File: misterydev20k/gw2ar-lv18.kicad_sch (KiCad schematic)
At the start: 55 parts, among them J3 JTAG, U10 TLV62569DBV, U11 TLV62569DBV, U5 GW2AR-LV18-QN88, U6 W25Q128JVS, U8 ME6211C33M5, U9 ME6211C33M5, Y2 27MHz

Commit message: Some dev board progress
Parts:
- removed JP4: VCCO_5, Jumper:SolderJumper-2_P1.3mm_Bridged_RoundedPad1.0x1.5mm, symbol Jumper:SolderJumper_2_Bridged
- removed JP5: VCC33, Jumper:SolderJumper-2_P1.3mm_Bridged_RoundedPad1.0x1.5mm, symbol Jumper:SolderJumper_2_Bridged
- removed JP6: +1V0, Jumper:SolderJumper-2_P1.3mm_Bridged_RoundedPad1.0x1.5mm, symbol Jumper:SolderJumper_2_Bridged
- JP3: value VCCO_4 -> ~{CFG}
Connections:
- net +1V0: now also FB2.2
- net VCC33: now also FB1.2
- net VCCO_4: now also C34.2, U8.5 (V_{OUT}); no longer JP3.2 (B)
- net VCCO_5: now also C36.2, U9.5 (V_{OUT})
- net at R40.2, U5.9 (IOR31B/~{RECONFIG}): now also JP3.2 (B)
- new net ~{CFG}: JP3.1 (A)
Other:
- note removed: "JP5, JP6 etc are used to isolate the FPGA during initial bringup."
- moved on the sheet: J3, R18

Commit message: More updates in dev20k
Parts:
- removed C37: 100nF, Capacitor_SMD:C_0402_1005Metric, symbol Device:C_Small
- removed C38: 10uF, Capacitor_SMD:C_0402_1005Metric, symbol Device:C_Small
- removed FB1: MPZ1608S101, Inductor_SMD:L_0603_1608Metric, symbol Device:FerriteBead
- removed L1: 2.2uH, Inductor_SMD:L_0805_2012Metric, symbol Device:L
- removed R36: 68k, Resistor_SMD:R_0402_1005Metric, symbol Device:R_Small
- removed R37: 15k, Resistor_SMD:R_0402_1005Metric, symbol Device:R_Small
- removed U10: TLV62569DBV, Package_TO_SOT_SMD:SOT-23-5, symbol Regulator_Switching:TLV62569DBV
- added C4, C46, C47, C48, C49, C50: 100nF, Capacitor_SMD:C_0402_1005Metric, symbol Device:C_Small
- added R26, R52: 22, Resistor_SMD:R_0402_1005Metric, symbol Device:R_Small
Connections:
- net GND: now also C4.1, C46.1, C47.1, C48.1, C49.1, C50.1
- net SD_CLK: now also R26.2, R52.2; no longer JP13.1 (A), JP13.2 (B)
- net VCC33: no longer C15.1, C27.1, R29.2, R31.2, R32.2, U5.12 (VCCX/VCC0_2/6/7), U5.3 (VCCX/VCC0_2/6/7), U5.58 (VCC0_3), U5.64 (VCCX/VCC0_2/6/7), U5.67 (VCC0_1), U5.78 (VCC0_0), U6.8 (VCC), Y2.1 (~{ST}), Y2.4 (Vcc)
- new net: JP13.1 (A), R26.1
- new net +3.3V: C15.1, C27.1, C4.2, C46.2, C47.2, C48.2, C49.2, C50.2, R29.2, R31.2, R32.2, U5.12 (VCCX/VCC0_2/6/7), U5.3 (VCCX/VCC0_2/6/7), U5.58 (VCC0_3), U5.64 (VCCX/VCC0_2/6/7), U5.67 (VCC0_1), U5.78 (VCC0_0), U6.8 (VCC), Y2.1 (~{ST}), Y2.4 (Vcc)
- new net Interfaces/SD_CLK: JP13.2 (B), R52.1
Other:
- note removed: "https://github.com/TomSimkin/UART_Verilog/blob/main/Tang_Nano_20K_3921_Schematics.pdf"
- moved on the sheet: C39, C40, FB2, L2, R38, R39, U11

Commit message: Update missing files
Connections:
- net SD_CLK: no longer R26.2
- new net SD_CLK_PI: R26.2
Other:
- sheet Interfaces ports: added ~{SD_DET}; removed none
- moved on the sheet: JP11, JP12, JP13, JP14, R26, R52

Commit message: Another board update
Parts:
- removed C40: 10uF, Capacitor_SMD:C_0402_1005Metric, symbol Device:C_Small
- removed FB2: MPZ1608S101, Inductor_SMD:L_0603_1608Metric, symbol Device:FerriteBead
- removed L2: 2.2uH, Inductor_SMD:L_0805_2012Metric, symbol Device:L
- removed U11: TLV62569DBV, Package_TO_SOT_SMD:SOT-23-5, symbol Regulator_Switching:TLV62569DBV
- removed U8, U9: ME6211C33M5, Package_TO_SOT_SMD:SOT-23-5, symbol Regulator_Linear:ME6211C33M5
- added C37: 22pF, Capacitor_SMD:C_0402_1005Metric, symbol Device:C_Small
- added C38: 22uF, Capacitor_SMD:C_0603_1608Metric, symbol Device:C_Small
- added L1: 3.3uH, Inductor_SMD:L_Sunlord_MWSA0402S, symbol Device:L
- added R37: 47k, Resistor_SMD:R_0402_1005Metric, symbol Device:R_Small
- added R56: 18k 1%, Resistor_SMD:R_0402_1005Metric, symbol Device:R_Small
- added U8: SY8113BADC, Package_TO_SOT_SMD:TSOT-23-6, symbol Regulator_Switching:LM2842Y
- C33: value 100nF -> 10uF; footprint Capacitor_SMD:C_0402_1005Metric -> Capacitor_SMD:C_0603_1608Metric; LCSC C1525 -> C52923
- C34, C39: footprint Capacitor_SMD:C_0402_1005Metric -> Capacitor_SMD:C_0603_1608Metric
- R38: value 10k -> 30k; LCSC (none) -> C11702
- R39: value 15k -> 12k 1%
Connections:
- net +1V0: now also C39.1, R39.2, C37.2, C38.1, L1.2
- net +3.3V: now also C16.2, C17.2, U5.23 (VCC0_5), U5.44 (VCC0_4)
- net +5V: now also C33.1, C34.1, R37.2, U8.5 (VIN); no longer C33.2, C35.2, C39.2
- net GND: now also C33.2, C34.2, C39.2, R38.1, C38.2, R56.1, U8.2 (GND); no longer C33.1, C34.1, C36.1, C39.1, R39.2
- net at R38.2: now also C35.2, R37.1, U8.4 (EN); no longer R39.1
- removed net VCCO_4: C17.2, C34.2, U5.44 (VCC0_4)
- removed net VCCO_5: C16.2, C36.2, U5.23 (VCC0_5)
- new net: C37.1, R39.1, R56.2, U8.3 (FB)
- new net: C36.1, U8.1 (BOOST)
- new net: C36.2, L1.1, U8.6 (SW)
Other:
- note added: "Vout = 0.6 * (1+R1/R2)"
- note removed: "or MT3520B"
- moved on the sheet: C4, C46, C47, C48, C49, C50

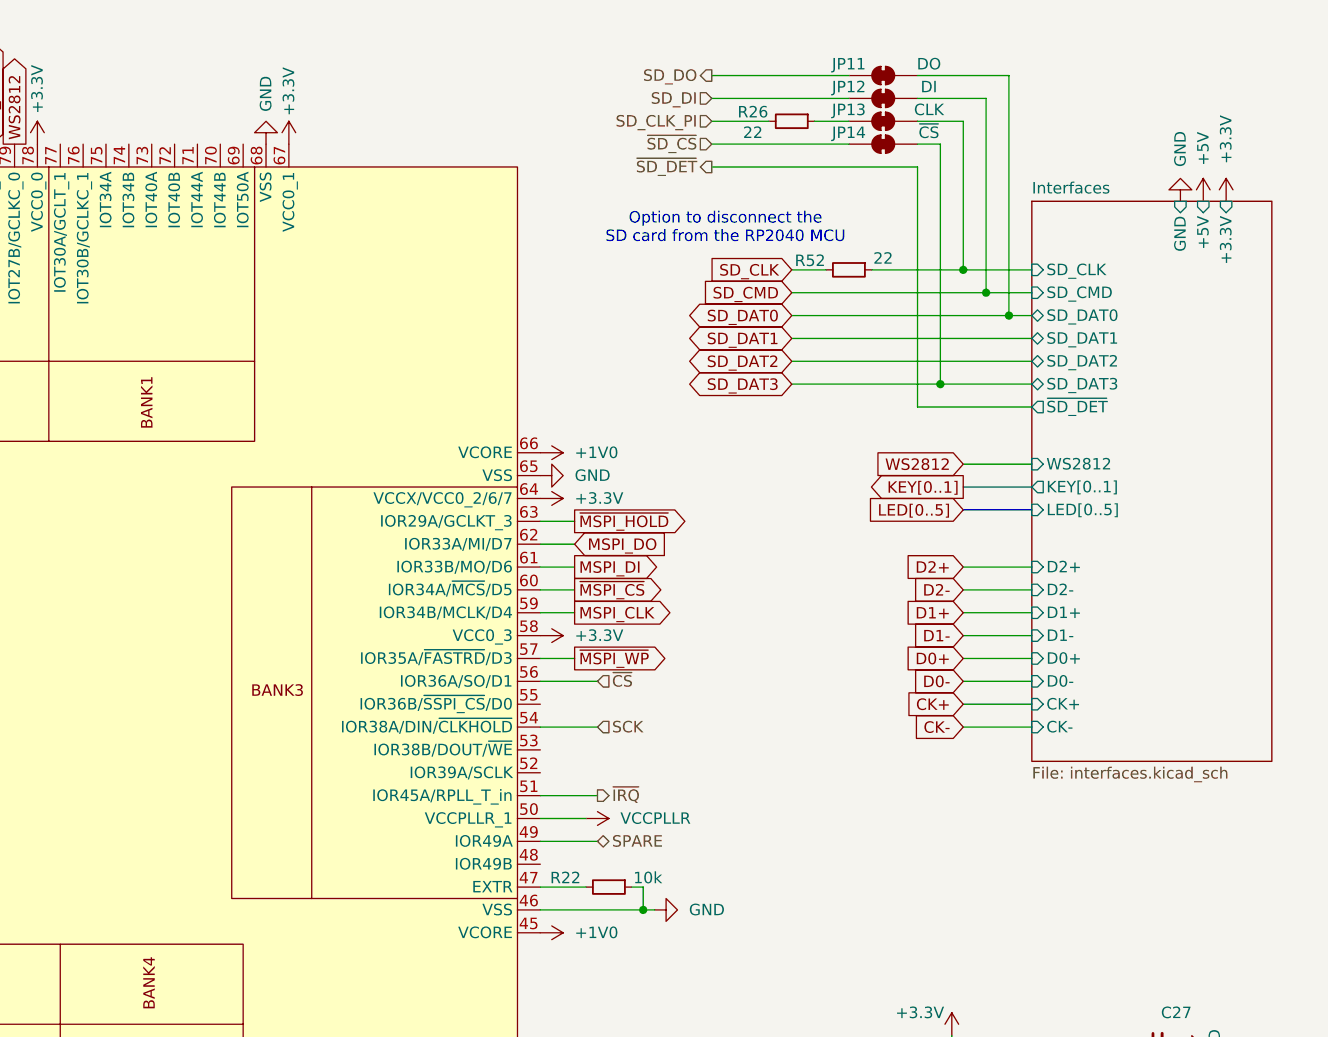
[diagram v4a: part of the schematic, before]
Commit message: Add grove connector for MIDI/UART
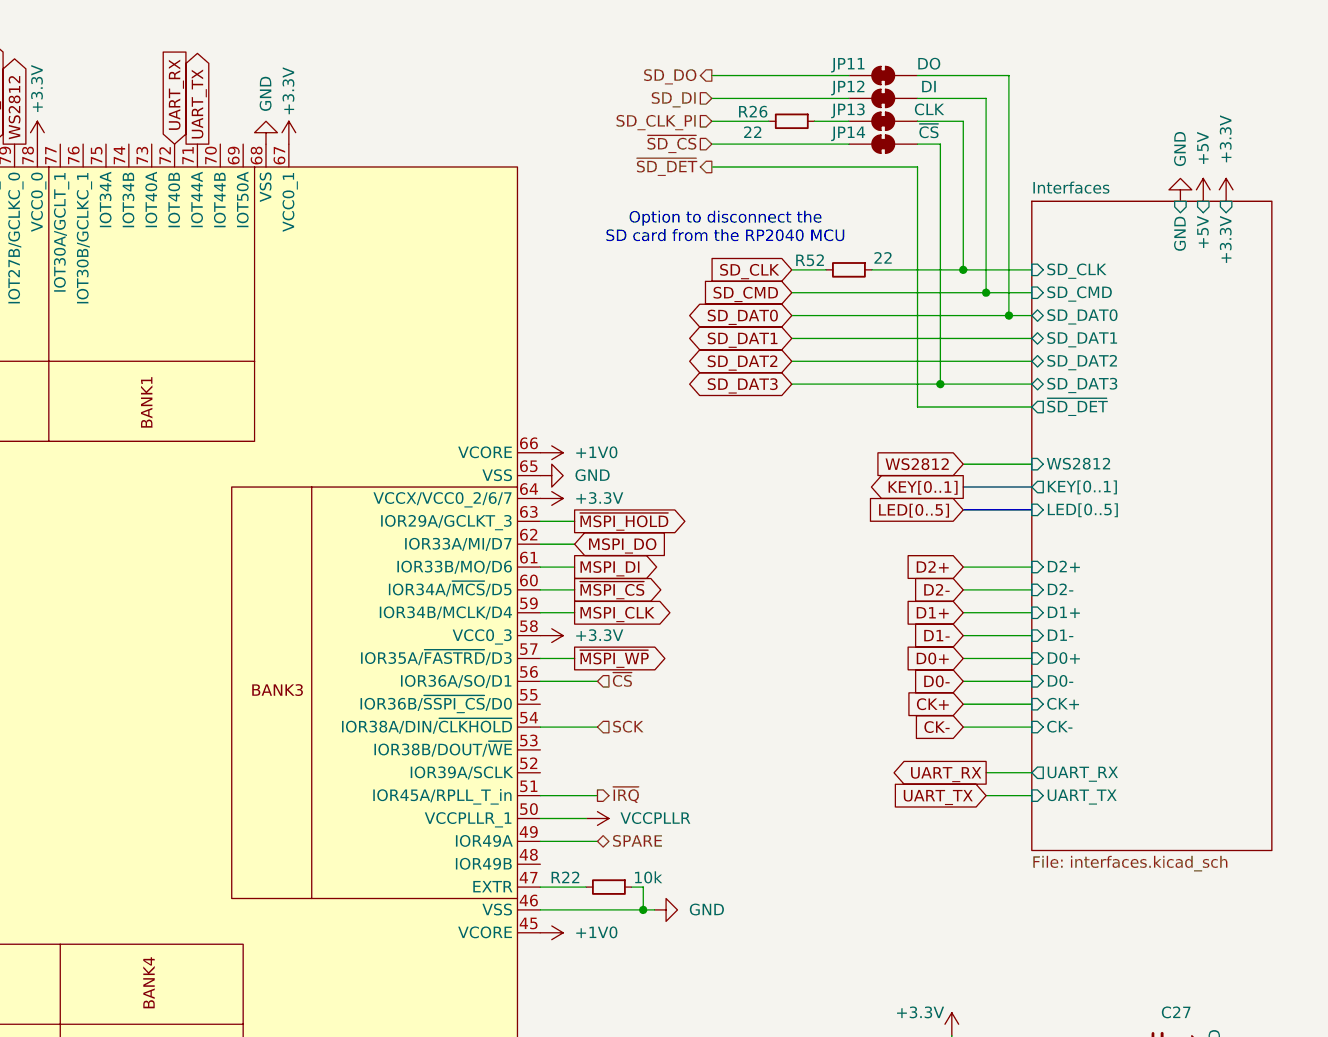
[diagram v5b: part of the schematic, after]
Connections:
- net UART_TX: now reaches U5.71 (IOT44A)
- net UART_RX: now reaches U5.72 (IOT40B)
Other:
- sheet Interfaces ports: added UART_RX, UART_TX; removed none
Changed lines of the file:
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@@
 	(wire
 		(pts
+			(xy 248.92 97.79) (xy 254 97.79)
+		)
+		(stroke
+			(width 0)
+			(type default)
+		)
+	)
+	(wire
+		(pts
 			(xy 64.77 127) (xy 73.66 127)
 		)
@@
 	(wire
 		(pts
+			(xy 248.92 100.33) (xy 254 100.33)
+		)
+		(stroke
+			(width 0)
+			(type default)
+		)
+	)
+	(wire
+		(pts
 			(xy 203.2 69.85) (xy 199.39 69.85)
 		)
@@
 		)
 	)
+	(global_label "UART_RX"
+		(shape input)
+		(at 158.75 27.94 90)
+		(fields_autoplaced yes)
+		(effects
+			(font
+				(size 1.27 1.27)
+			)
+			(justify left)
+		)
+		(property "Intersheetrefs" "${INTERSHEET_REFS}"
+			(at 158.75 17.5052 90)
+			(effects
+				(font
+					(size 1.27 1.27)
+				)
+				(justify left)
+				(hide yes)
+			)
+		)
+	)
+	(global_label "UART_RX"
+		(shape output)
+		(at 248.92 97.79 180)
+		(fields_autoplaced yes)
+		(effects
+			(font
+				(size 1.27 1.27)
+			)
+			(justify right)
+		)
+		(property "Intersheetrefs" "${INTERSHEET_REFS}"
+			(at 238.4852 97.79 0)
+			(effects
+				(font
+					(size 1.27 1.27)
+				)
+				(justify right)
+				(hide yes)
+			)
+		)
+	)
 	(global_label "D1+"
 		(shape output)
@@
 		)
 	)
+	(global_label "UART_TX"
+		(shape input)
+		(at 248.92 100.33 180)
+		(fields_autoplaced yes)
+		(effects
+			(font
+				(size 1.27 1.27)
+			)
+			(justify right)
+		)
+		(property "Intersheetrefs" "${INTERSHEET_REFS}"
+			(at 238.7876 100.33 0)
+			(effects
+				(font
+					(size 1.27 1.27)
+				)
+				(justify right)
+				(hide yes)
+			)
+		)
+	)
 	(global_label "MSPI_DI"
 		(shape input)
@@
 		)
 	)
+	(global_label "UART_TX"
+		(shape output)
+		(at 161.29 27.94 90)
+		(fields_autoplaced yes)
+		(effects
+			(font
+				(size 1.27 1.27)
+			)
+			(justify left)
+		)
+		(property "Intersheetrefs" "${INTERSHEET_REFS}"
+			(at 161.29 17.8076 90)
+			(effects
+				(font
+					(size 1.27 1.27)
+				)
+				(justify left)
+				(hide yes)
+			)
+		)
+	)
 	(global_label "MSPI_DO"
 		(shape output)
@@
 	(sheet
 		(at 254 34.29)
-		(size 26.67 62.23)
+		(size 26.67 72.136)
 		(exclude_from_sim no)
 		(in_bom yes)
@@
 		)
 		(property "Sheetfile" "interfaces.kicad_sch"
-			(at 254 97.1046 0)
+			(at 254 107.0106 0)
 			(effects
 				(font
@@
 			(effects
 				(font
+					(size 1.27 1.27)
+				)
+				(justify left)
+			)
+		)
+		(pin "UART_RX" output
+			(at 254 97.79 180)
+			(effects
+				(font
+					(size 1.27 1.27)
+				)
+				(justify left)
+			)
+		)
+		(pin "UART_TX" input
+			(at 254 100.33 180)
+			(effects
+				(font

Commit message: Update board
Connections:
- net JOYA2: now reaches U5.25 (IOB6A)
- net JOYA3: now reaches U5.26 (IOB6B)
- net JOYA0: now reaches U5.27 (IOB8A)
- net JOYA1: now reaches U5.28 (IOB8B)
- net JOYA4: now reaches U5.29 (IOB14A)
- net JOYA5: now reaches U5.30 (IOB14B)
- net JOYB3: now reaches U5.31 (IOB18A)
- net JOYB0: now reaches U5.73 (IOT40A)
- net JOYB1: now reaches U5.74 (IOT34B)
- net JOYB2: now reaches U5.77 (IOT30A/GCLT_1)
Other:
- sheet Interfaces ports: added JOYA[0..5], JOYB[0..5]; removed none

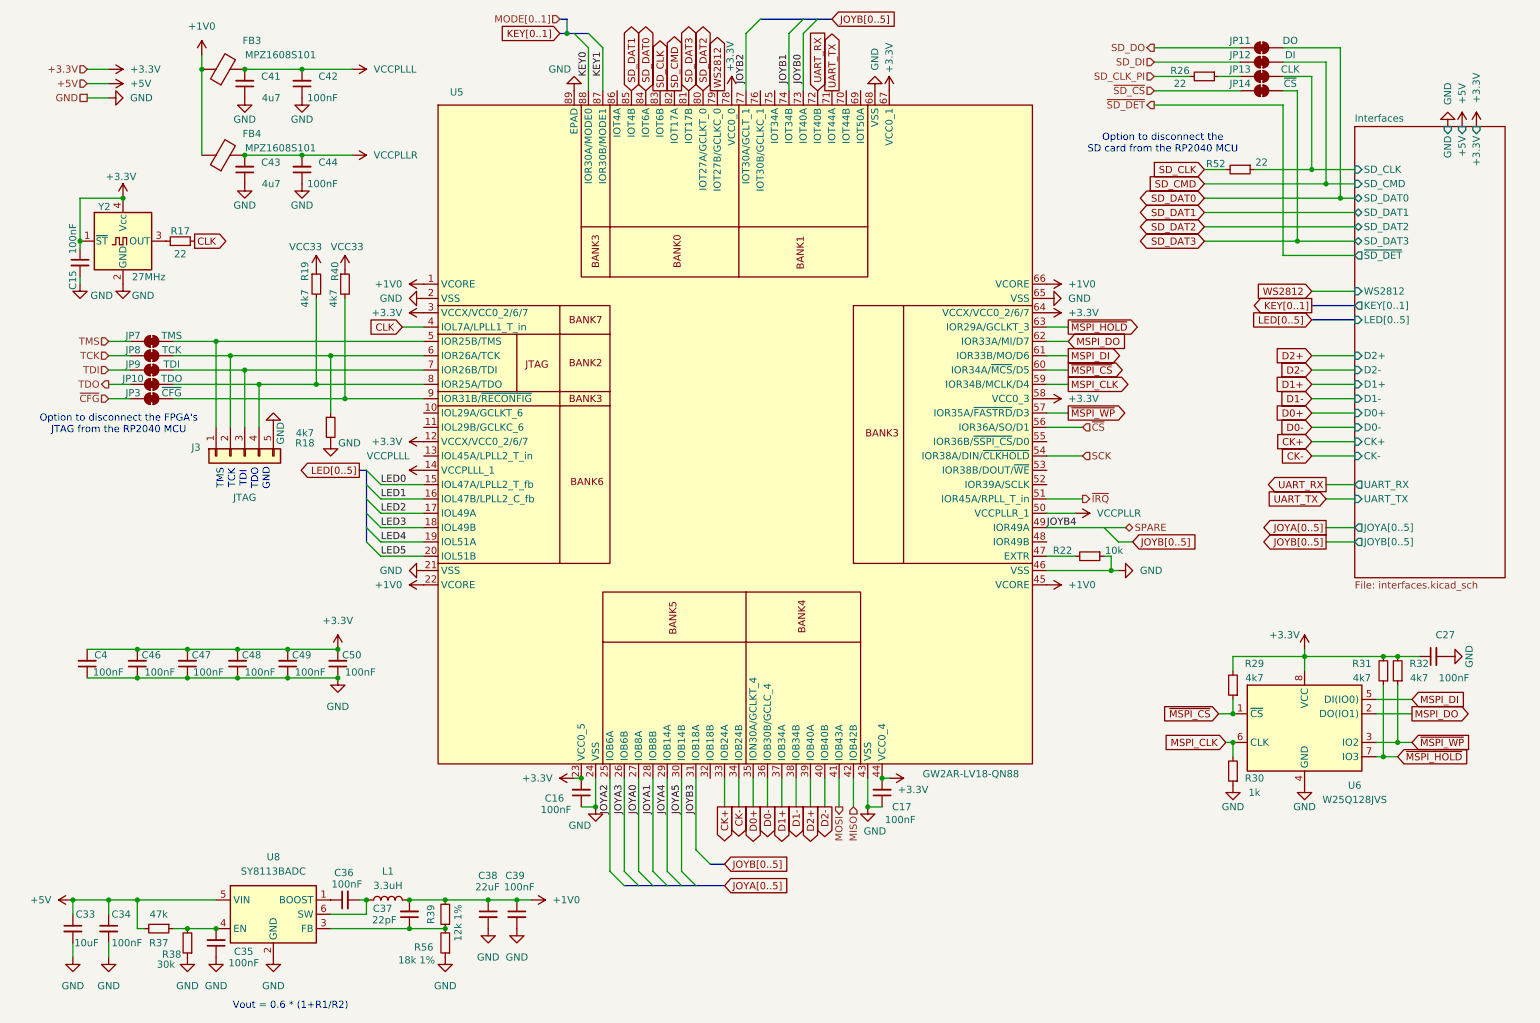
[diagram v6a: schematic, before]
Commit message: Fix dev20k schematic
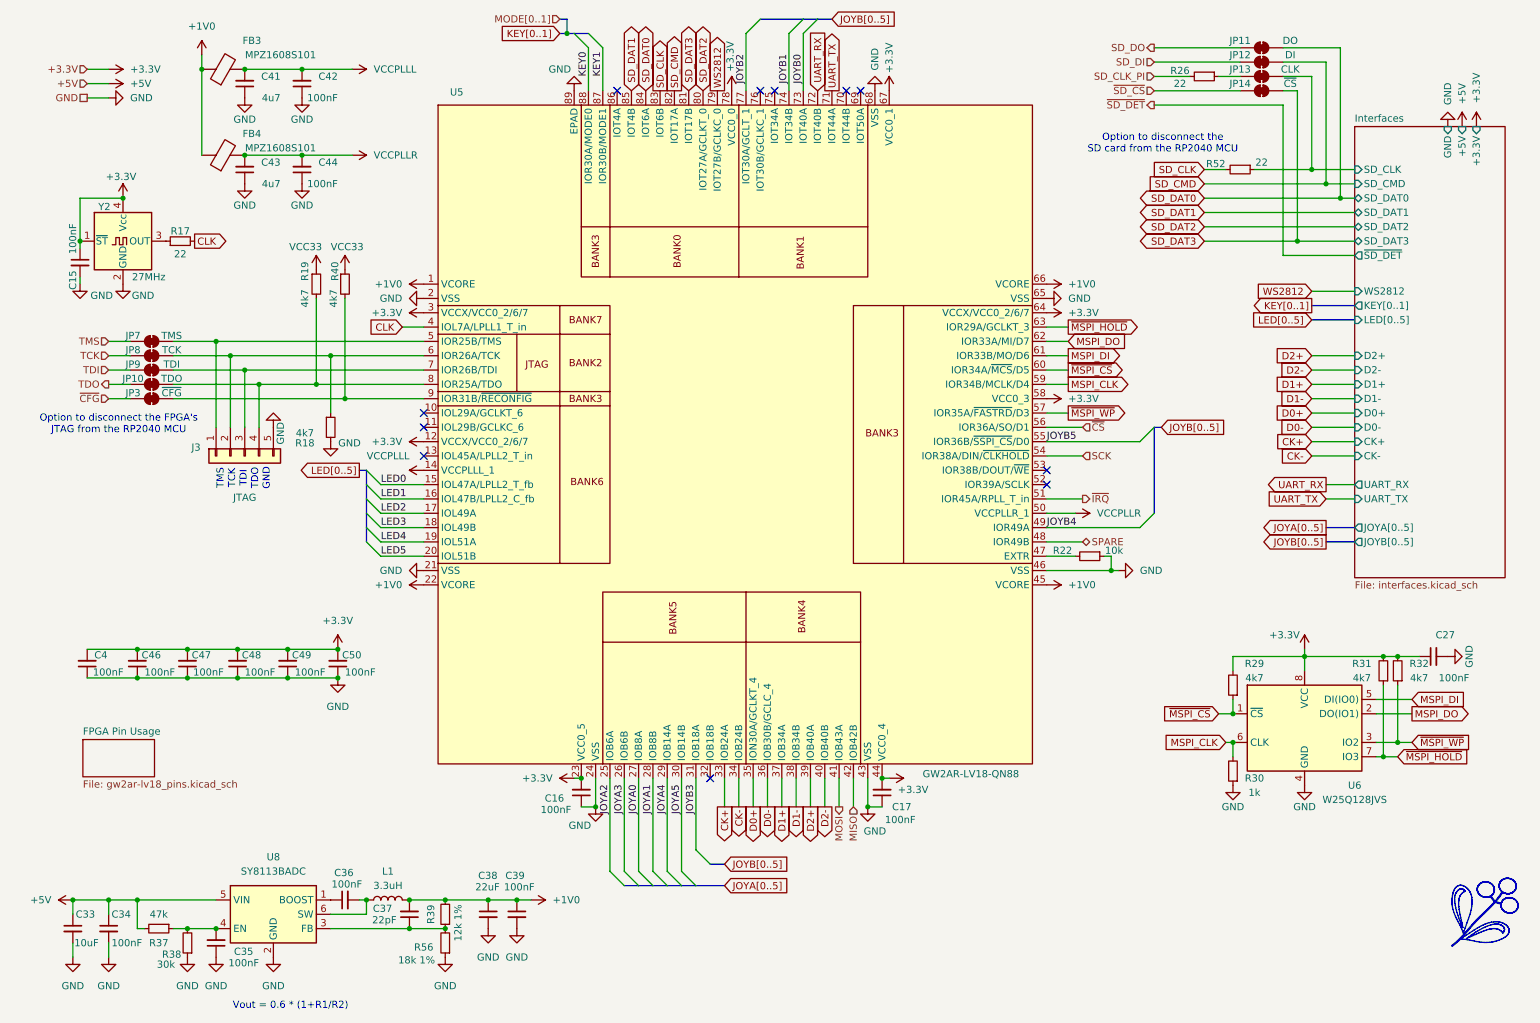
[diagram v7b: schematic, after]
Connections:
- net SPARE: now also U5.48 (IOR49B); no longer U5.49 (IOR49A)
- net JOYB5: now reaches U5.55 (IOR36B/~{SSPI_CS}/D0)
- new net JOYB4: U5.49 (IOR49A)
- no-connect marks 0 -> 11
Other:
- added sheet FPGA Pin Usage (gw2ar-lv18_pins.kicad_sch)
- company: (none) -> Till Harbaum
- title: (none) -> MiSTeryDev 20k - GW2AR-LV18 FPGA

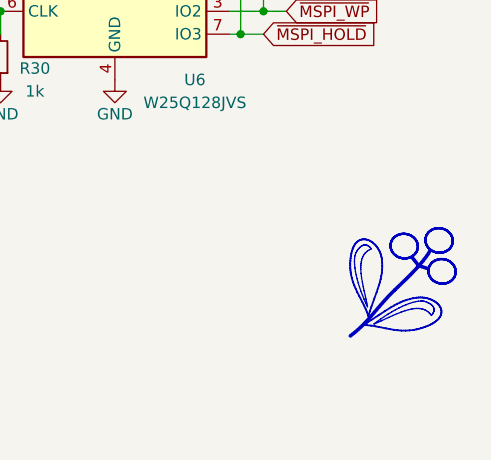
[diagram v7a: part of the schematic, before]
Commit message: Update pin table
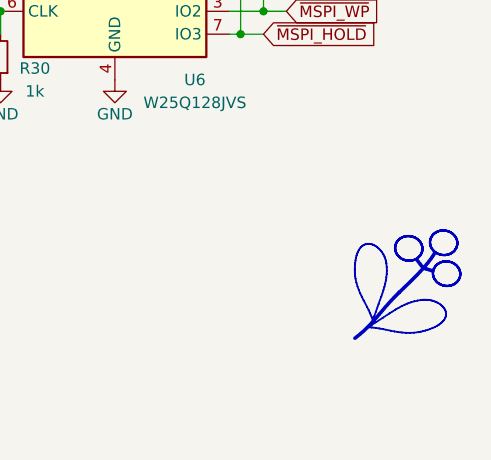
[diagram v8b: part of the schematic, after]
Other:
- title: MiSTeryDev 20k - GW2AR-LV18 FPGA -> MiSTle - MiSTeryDev20k
